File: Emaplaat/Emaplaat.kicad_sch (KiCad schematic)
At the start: 15 parts, among them IC1 ESP32-S3-WROOM-2-N32R16V, IC13 74HC595PW-Q100,118, IC7 74HC595PW-Q100,118

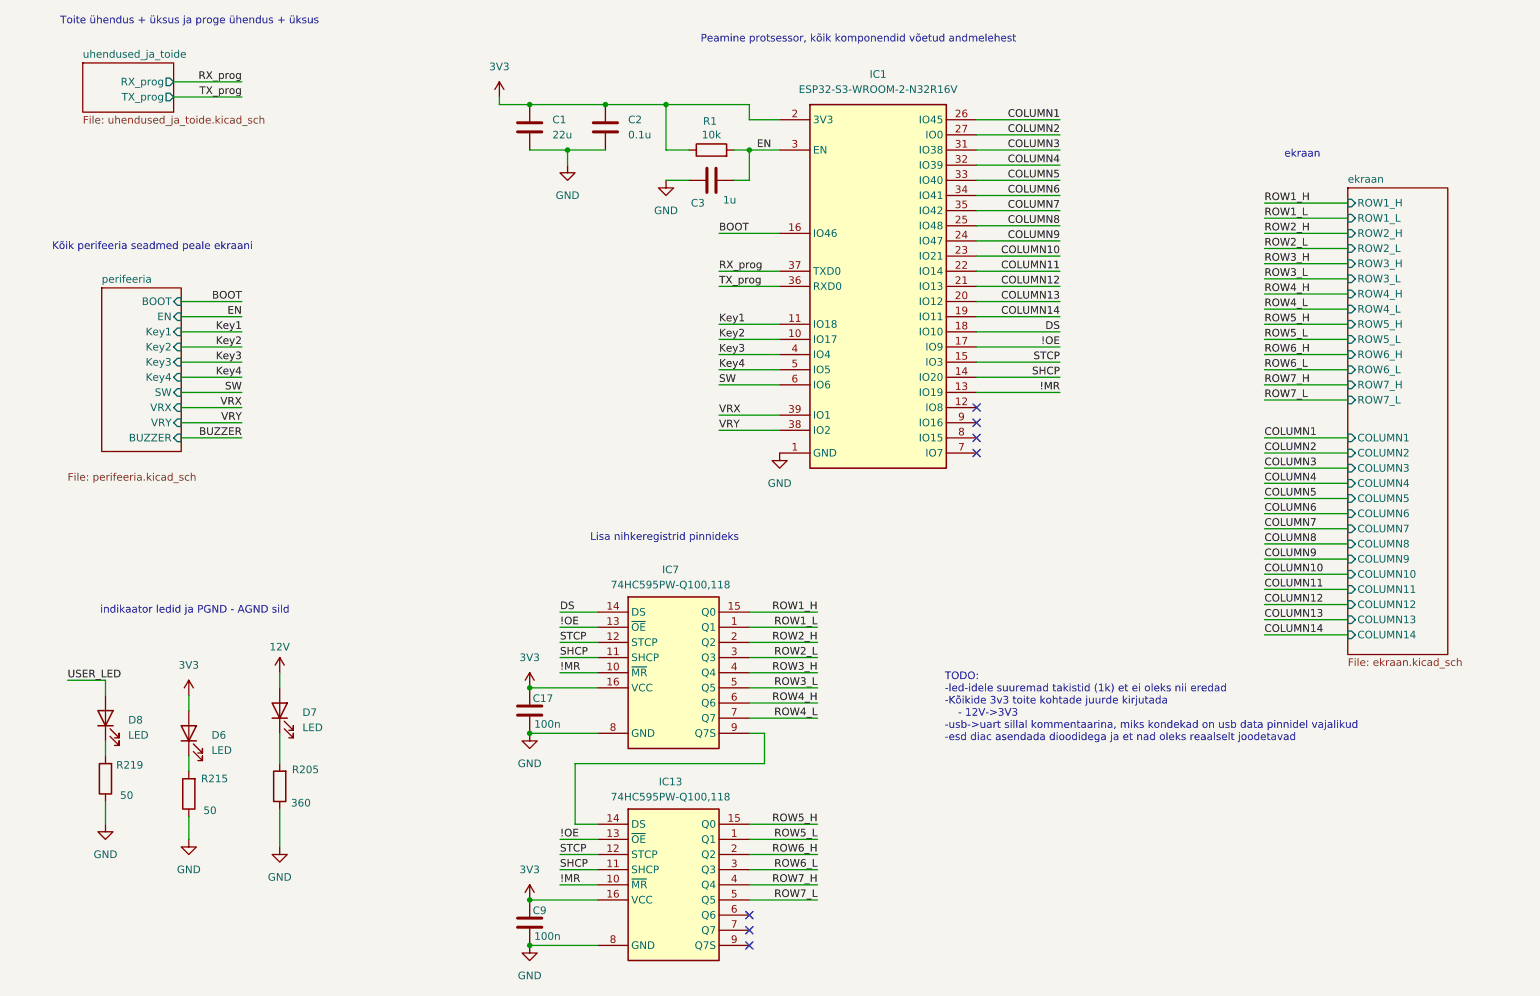
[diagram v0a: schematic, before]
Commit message: 3V3 voolud kontrollitud
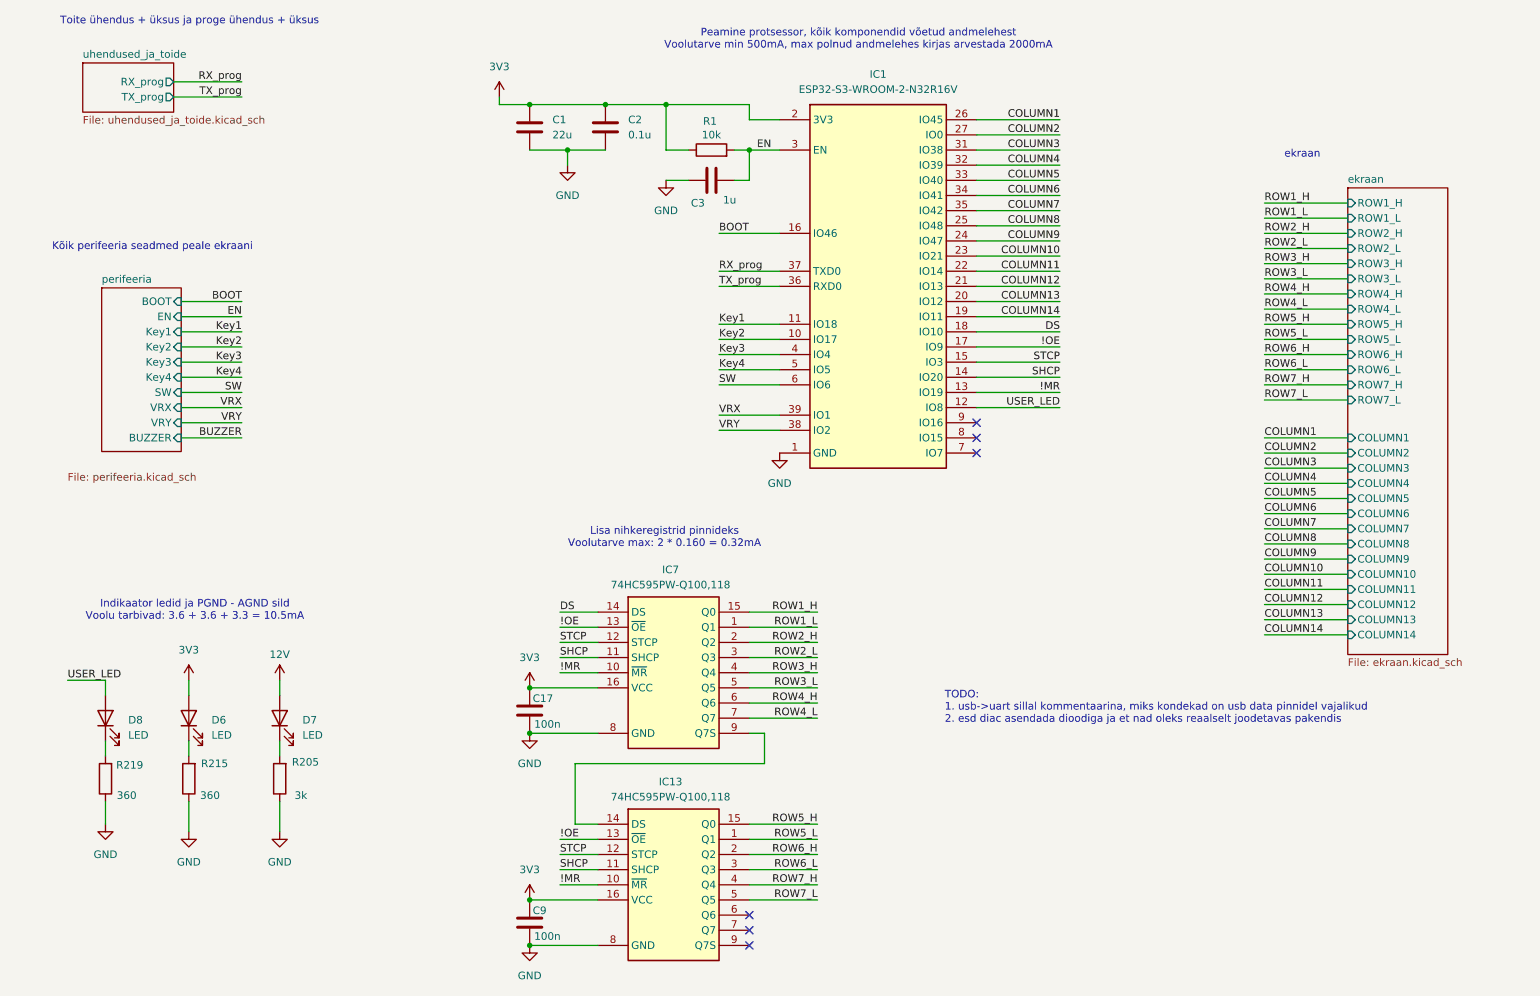
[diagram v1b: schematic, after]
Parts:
- R205: value 360 -> 3k
- R215, R219: value 50 -> 360
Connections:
- net USER_LED: now also IC1.12 (IO8)
- no-connect marks 7 -> 6
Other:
- note added: "Indikaator ledid ja PGND - AGND sild Voolu tarbivad: 3.6 + 3.6 + 3.3 = 10.5mA"
- note added: "Lisa nihkeregistrid pinnideks Voolutarve max: 2 * 0.160 = 0.32mA"
- note added: "Peamine protsessor, kõik komponendid võetud andmelehest Voolutarve min 500mA, max polnud andmelehes kirjas arvestada 2000mA"
- note added: "TODO: 1. usb->uart sillal kommentaarina, miks kondekad on usb data pinnidel vajalikud 2. esd diac asendada dioodiga ja et nad oleks reaalselt joodetavas pakendis"
- note removed: "Lisa nihkeregistrid pinnideks"
- note removed: "Peamine protsessor, kõik komponendid võetud andmelehest"
- note removed: "TODO: -led-idele suuremad takistid (1k) et ei oleks nii eredad -Kõikide 3v3 toite kohtade juurde kirjutada - 12V->3V3 -usb->uart sillal kommentaarina, miks kondekad on usb data pinnidel vajalikud -esd diac asendada dioodidega ja et nad oleks reaalselt joodetavad"
- note removed: "indikaator ledid ja PGND - AGND sild"
- moved on the sheet: D6, D7, R205, R215
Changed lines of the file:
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@@
 		)
 	)
-	(text "indikaator ledid ja PGND - AGND sild"
+	(text "Indikaator ledid ja PGND - AGND sild\nVoolu tarbivad: 3.6 + 3.6 + 3.3 = 10.5mA"
 		(exclude_from_sim no)
 		(at 53.086 128.016 0)
@@
 		)
 	)
-	(text "Peamine protsessor, kõik komponendid võetud andmelehest"
+	(text "Peamine protsessor, kõik komponendid võetud andmelehest\nVoolutarve min 500mA, max polnud andmelehes kirjas arvestada 2000mA"
 		(exclude_from_sim no)
 		(at 164.338 32.258 0)
@@
 		)
 	)
-	(text "Lisa nihkeregistrid pinnideks"
+	(text "Lisa nihkeregistrid pinnideks\nVoolutarve max: 2 * 0.160 = 0.32mA"
 		(exclude_from_sim no)
 		(at 131.826 115.824 0)
@@
 		)
 	)
-	(text "TODO:\n-led-idele suuremad takistid (1k) et ei oleks nii eredad\n-Kõikide 3v3 toite kohtade juurde kirjutada\n    - 12V->3V3\n-usb->uart sillal kommentaarina, miks kondekad on usb data pinnidel vajalikud\n-esd diac asendada dioodidega ja et nad oleks reaalselt joodetavad\n"
+	(text "TODO:\n1. usb->uart sillal kommentaarina, miks kondekad on usb data pinnidel vajalikud\n2. esd diac asendada dioodiga ja et nad oleks reaalselt joodetavas pakendis\n"
 		(exclude_from_sim no)
 		(at 178.816 144.272 0)
@@
 	)
 	(no_connect
-		(at 184.15 93.98)
-	)
-	(no_connect
 		(at 184.15 96.52)
 	)
@@
 	(wire
 		(pts
-			(xy 67.31 148.59) (xy 67.31 153.67)
+			(xy 67.31 149.86) (xy 67.31 152.4)
 		)
 		(stroke
@@
 	(wire
 		(pts
-			(xy 67.31 161.29) (xy 67.31 167.64)
+			(xy 67.31 160.02) (xy 67.31 165.1)
 		)
 		(stroke
@@
 	(wire
 		(pts
+			(xy 184.15 93.98) (xy 198.12 93.98)
+		)
+		(stroke
+			(width 0)
+			(type default)
+		)
+	)
+	(wire
+		(pts
 			(xy 232.41 67.31) (xy 246.38 67.31)
 		)
@@
 	(wire
 		(pts
-			(xy 67.31 138.43) (xy 67.31 140.97)
+			(xy 67.31 139.7) (xy 67.31 142.24)
 		)
 		(stroke
@@
 	(wire
 		(pts
-			(xy 52.07 152.4) (xy 52.07 154.94)
+			(xy 52.07 149.86) (xy 52.07 152.4)
 		)
 		(stroke
@@
 	(wire
 		(pts
-			(xy 52.07 162.56) (xy 52.07 166.37)
+			(xy 52.07 160.02) (xy 52.07 165.1)
 		)
 		(stroke
@@
 	(wire
 		(pts
-			(xy 52.07 144.78) (xy 52.07 142.24)
+			(xy 52.07 142.24) (xy 52.07 139.7)
 		)
 		(stroke
@@
 		)
 	)
+	(label "USER_LED"
+		(at 198.12 93.98 180)
+		(effects
+			(font
+				(size 1.27 1.27)
+			)
+			(justify right bottom)
+		)
+	)
 	(label "!MR"
 		(at 114.3 173.99 0)
@@
 	(symbol
 		(lib_id "power:VCC")
-		(at 67.31 138.43 0)
+		(at 67.31 139.7 0)
 		(unit 1)
 		(exclude_from_sim no)
@@
 		(dnp no)
 		(property "Reference" "#PWR0115"
-			(at 67.31 142.24 0)
+			(at 67.31 143.51 0)
 			(effects
 				(font
@@
 		)
 		(property "Value" "12V"
-			(at 67.31 134.112 0)
+			(at 67.31 135.382 0)
 			(effects
 				(font
@@
 		)
 		(property "Footprint" ""
-			(at 67.31 138.43 0)
+			(at 67.31 139.7 0)
 			(effects
 				(font
@@
 		)
 		(property "Datasheet" ""
-			(at 67.31 138.43 0)
+			(at 67.31 139.7 0)
 			(effects
 				(font
@@
 		)
 		(property "Description" "Power symbol creates a global label with name \"VCC\""
-			(at 67.31 138.43 0)
+			(at 67.31 139.7 0)
 			(effects
 				(font
@@
 	(symbol
 		(lib_id "Device:R")
-		(at 52.07 158.75 180)
+		(at 52.07 156.21 180)
 		(unit 1)
 		(exclude_from_sim no)
@@
 		(dnp no)
 		(property "Reference" "R215"
-			(at 56.388 156.21 0)
+			(at 56.388 153.67 0)
 			(effects
 				(font
@@
 			)
 		)
-		(property "Value" "50"
-			(at 55.626 161.544 0)
+		(property "Value" "360"
+			(at 55.626 159.004 0)
 			(effects
 				(font
@@
 		)
 		(property "Footprint" "Resistor_SMD:R_0603_1608Metric"
-			(at 53.848 158.75 90)
+			(at 53.848 156.21 90)
 			(effects
 				(font
@@
 		)
 		(property "Datasheet" "~"
-			(at 52.07 158.75 0)
+			(at 52.07 156.21 0)
 			(effects
 				(font
@@
 		)
 		(property "Description" "Resistor"
-			(at 52.07 158.75 0)
+			(at 52.07 156.21 0)
 			(effects
 				(font
@@
 	(symbol
 		(lib_id "Device:LED")
-		(at 52.07 148.59 90)
+		(at 52.07 146.05 90)
 		(unit 1)
 		(exclude_from_sim no)
@@
 		(dnp no)
 		(property "Reference" "D6"
-			(at 55.88 148.9074 90)
+			(at 55.88 146.3674 90)
 			(effects
 				(font
@@
 		)
 		(property "Value" "LED"
-			(at 55.88 151.4474 90)
+			(at 55.88 148.9074 90)
 			(effects
 				(font
@@
 		)
 		(property "Footprint" "LED_SMD:LED_0603_1608Metric"
-			(at 52.07 148.59 0)
+			(at 52.07 146.05 0)
 			(effects
 				(font
@@
 		)
 		(property "Datasheet" "https://www.we-online.com/components/products/datasheet/150060YS75000.pdf"
-			(at 52.07 148.59 0)
+			(at 52.07 146.05 0)
 			(effects
 				(font
@@
 		)
 		(property "Description" "Light emitting diode"
-			(at 52.07 148.59 0)
+			(at 52.07 146.05 0)
 			(effects
 				(font
@@
 		)
 		(property "Sim.Pins" "1=K 2=A"
-			(at 52.07 148.59 0)
+			(at 52.07 146.05 0)
 			(effects
 				(font
@@
 	(symbol
 		(lib_id "power:GND")
-		(at 52.07 166.37 0)
+		(at 52.07 165.1 0)
 		(unit 1)
 		(exclude_from_sim no)
@@
 		(fields_autoplaced yes)
 		(property "Reference" "#PWR021"
-			(at 52.07 172.72 0)
+			(at 52.07 171.45 0)
 			(effects
 				(font
@@
 		)
 		(property "Value" "GND"
-			(at 52.07 171.45 0)
+			(at 52.07 170.18 0)
 			(effects
 				(font
@@
 		)
 		(property "Footprint" ""
-			(at 52.07 166.37 0)
+			(at 52.07 165.1 0)
 			(effects
 				(font
@@
 		)
 		(property "Datasheet" ""
-			(at 52.07 166.37 0)
+			(at 52.07 165.1 0)
 			(effects
 				(font
@@
 		)
 		(property "Description" "Power symbol creates a global label with name \"GND\" , ground"
-			(at 52.07 166.37 0)
+			(at 52.07 165.1 0)
 			(effects
 				(font
@@
 	(symbol
 		(lib_id "Device:R")
-		(at 67.31 157.48 180)
+		(at 67.31 156.21 180)
 		(unit 1)
 		(exclude_from_sim no)
@@
 		(dnp no)
 		(property "Reference" "R205"
-			(at 71.628 154.686 0)
+			(at 71.628 153.416 0)
 			(effects
 				(font
@@
 			)
 		)
-		(property "Value" "360"
-			(at 70.866 160.274 0)
+		(property "Value" "3k"
+			(at 70.866 159.004 0)
 			(effects
 				(font
@@
 		)
 		(property "Footprint" "Resistor_SMD:R_0603_1608Metric"
-			(at 69.088 157.48 90)
+			(at 69.088 156.21 90)
 			(effects
 				(font
@@
 		)
 		(property "Datasheet" "~"
-			(at 67.31 157.48 0)
+			(at 67.31 156.21 0)
 			(effects
 				(font
@@
 		)
 		(property "Description" "Resistor"
-			(at 67.31 157.48 0)
+			(at 67.31 156.21 0)
 			(effects
 				(font
@@
 	(symbol
 		(lib_id "power:GND")
-		(at 67.31 167.64 0)
+		(at 67.31 165.1 0)
 		(unit 1)
 		(exclude_from_sim no)
@@
 		(fields_autoplaced yes)
 		(property "Reference" "#PWR020"
-			(at 67.31 173.99 0)
+			(at 67.31 171.45 0)
 			(effects
 				(font
@@
 		)
 		(property "Value" "GND"
-			(at 67.31 172.72 0)
+			(at 67.31 170.18 0)
 			(effects
 				(font
@@
 		)
 		(property "Footprint" ""
-			(at 67.31 167.64 0)
+			(at 67.31 165.1 0)
 			(effects
 				(font
@@
 		)
 		(property "Datasheet" ""
-			(at 67.31 167.64 0)
+			(at 67.31 165.1 0)
 			(effects
 				(font
@@
 		)
 		(property "Description" "Power symbol creates a global label with name \"GND\" , ground"
-			(at 67.31 167.64 0)
+			(at 67.31 165.1 0)
 			(effects
 				(font
@@
 			)
 		)
-		(property "Value" "50"
+		(property "Value" "360"
 			(at 41.656 159.004 0)
 			(effects
@@
 	(symbol
 		(lib_id "Device:LED")
-		(at 67.31 144.78 90)
+		(at 67.31 146.05 90)
 		(unit 1)
 		(exclude_from_sim no)
@@
 		(fields_autoplaced yes)
 		(property "Reference" "D7"
-			(at 71.12 145.0974 90)
+			(at 71.12 146.3674 90)
 			(effects
 				(font
@@
 		)
 		(property "Value" "LED"
-			(at 71.12 147.6374 90)
+			(at 71.12 148.9074 90)
 			(effects
 				(font
@@
 		)
 		(property "Footprint" "LED_SMD:LED_0603_1608Metric"
-			(at 67.31 144.78 0)
+			(at 67.31 146.05 0)
 			(effects
 				(font
@@
 		)
 		(property "Datasheet" "https://www.we-online.com/components/products/datasheet/150060YS75000.pdf"
-			(at 67.31 144.78 0)
+			(at 67.31 146.05 0)
 			(effects
 				(font
@@
 		)
 		(property "Description" "Light emitting diode"
-			(at 67.31 144.78 0)
+			(at 67.31 146.05 0)
 			(effects
 				(font
@@
 		)
 		(property "Sim.Pins" "1=K 2=A"
-			(at 67.31 144.78 0)
+			(at 67.31 146.05 0)
 			(effects
 				(font
@@
 	(symbol
 		(lib_id "power:VCC")
-		(at 52.07 142.24 0)
+		(at 52.07 139.7 0)
 		(unit 1)
 		(exclude_from_sim no)
@@
 		(fields_autoplaced yes)
 		(property "Reference" "#PWR0113"
-			(at 52.07 146.05 0)
+			(at 52.07 143.51 0)
 			(effects
 				(font
@@
 		)
 		(property "Value" "3V3"
-			(at 52.07 137.16 0)
+			(at 52.07 134.62 0)
 			(effects
 				(font
@@
 		)
 		(property "Footprint" ""
-			(at 52.07 142.24 0)
+			(at 52.07 139.7 0)
 			(effects
 				(font
@@
 		)
 		(property "Datasheet" ""
-			(at 52.07 142.24 0)
+			(at 52.07 139.7 0)
 			(effects
 				(font
@@
 		)
 		(property "Description" "Power symbol creates a global label with name \"VCC\""
-			(at 52.07 142.24 0)
+			(at 52.07 139.7 0)
 			(effects
 				(font

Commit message: Kaareli kolmas tagasiside
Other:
- note removed: "TODO: 1. usb->uart sillal kommentaarina, miks kondekad on usb data pinnidel vajalikud 2. esd diac asendada dioodiga ja et nad oleks reaalselt joodetavas pakendis"
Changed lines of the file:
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@@
-		)
-	)
-	(text "TODO:\n1. usb->uart sillal kommentaarina, miks kondekad on usb data pinnidel vajalikud\n2. esd diac asendada dioodiga ja et nad oleks reaalselt joodetavas pakendis\n"
-		(exclude_from_sim no)
-		(at 178.816 144.272 0)
-		(effects
-			(font
-				(size 1.27 1.27)
-			)
-			(justify left)
 		)
 	)

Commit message: jajald
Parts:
- C1, C2, C3: footprint (none) -> Capacitor_SMD:C_0603_1608Metric_Pad1.08x0.95mm_HandSolder
- C4: renamed from C17; footprint (none) -> Capacitor_SMD:C_0603_1608Metric_Pad1.08x0.95mm_HandSolder
- C5: renamed from C9; footprint (none) -> Capacitor_SMD:C_0603_1608Metric_Pad1.08x0.95mm_HandSolder
- D1: renamed from D8; footprint LED_SMD:LED_0603_1608Metric -> LED_SMD:LED_0603_1608Metric_Pad1.05x0.95mm_HandSolder
- D2: renamed from D6; footprint LED_SMD:LED_0603_1608Metric -> LED_SMD:LED_0603_1608Metric_Pad1.05x0.95mm_HandSolder
- D3: renamed from D7; footprint LED_SMD:LED_0603_1608Metric -> LED_SMD:LED_0603_1608Metric_Pad1.05x0.95mm_HandSolder
- R1: footprint (none) -> Resistor_SMD:R_0603_1608Metric_Pad0.98x0.95mm_HandSolder
- R2: renamed from R219; footprint Resistor_SMD:R_0603_1608Metric -> Resistor_SMD:R_0603_1608Metric_Pad0.98x0.95mm_HandSolder
- R3: renamed from R215; footprint Resistor_SMD:R_0603_1608Metric -> Resistor_SMD:R_0603_1608Metric_Pad0.98x0.95mm_HandSolder
- R4: renamed from R205; footprint Resistor_SMD:R_0603_1608Metric -> Resistor_SMD:R_0603_1608Metric_Pad0.98x0.95mm_HandSolder
- renumbered IC7 to IC2, IC13 to IC3
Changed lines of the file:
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@@
 			)
 		)
-		(property "Footprint" ""
+		(property "Footprint" "Capacitor_SMD:C_0603_1608Metric_Pad1.08x0.95mm_HandSolder"
 			(at 110.1852 50.8 0)
 			(effects
@@
 		(on_board yes)
 		(dnp no)
-		(property "Reference" "D8"
+		(property "Reference" "D1"
 			(at 41.91 146.3674 90)
 			(effects
@@
 			)
 		)
-		(property "Footprint" "LED_SMD:LED_0603_1608Metric"
+		(property "Footprint" "LED_SMD:LED_0603_1608Metric_Pad1.05x0.95mm_HandSolder"
 			(at 38.1 146.05 0)
 			(effects
@@
 			(project "Emaplaat"
 				(path "/489224c0-ace1-4530-aa61-a5d03adf1434"
-					(reference "D8")
+					(reference "D1")
 					(unit 1)
 				)
@@
 			)
 		)
-		(property "Footprint" ""
+		(property "Footprint" "Capacitor_SMD:C_0603_1608Metric_Pad1.08x0.95mm_HandSolder"
 			(at 122.8852 50.8 0)
 			(effects
@@
 		(dnp no)
 		(fields_autoplaced yes)
-		(property "Reference" "IC7"
+		(property "Reference" "IC2"
 			(at 132.842 121.158 0)
 			(effects
@@
 			(project "Emaplaat"
 				(path "/489224c0-ace1-4530-aa61-a5d03adf1434"
-					(reference "IC7")
+					(reference "IC2")
 					(unit 1)
 				)
@@
 		(on_board yes)
 		(dnp no)
-		(property "Reference" "R215"
+		(property "Reference" "R3"
 			(at 56.388 153.67 0)
 			(effects
@@
 			)
 		)
-		(property "Footprint" "Resistor_SMD:R_0603_1608Metric"
+		(property "Footprint" "Resistor_SMD:R_0603_1608Metric_Pad0.98x0.95mm_HandSolder"
 			(at 53.848 156.21 90)
 			(effects
@@
 			(project "Emaplaat"
 				(path "/489224c0-ace1-4530-aa61-a5d03adf1434"
-					(reference "R215")
+					(reference "R3")
 					(unit 1)
 				)
@@
 		(on_board yes)
 		(dnp no)
-		(property "Reference" "D6"
+		(property "Reference" "D2"
 			(at 55.88 146.3674 90)
 			(effects
@@
 			)
 		)
-		(property "Footprint" "LED_SMD:LED_0603_1608Metric"
+		(property "Footprint" "LED_SMD:LED_0603_1608Metric_Pad1.05x0.95mm_HandSolder"
 			(at 52.07 146.05 0)
 			(effects
@@
 			(project "Emaplaat"
 				(path "/489224c0-ace1-4530-aa61-a5d03adf1434"
-					(reference "D6")
+					(reference "D2")
 					(unit 1)
 				)
@@
 			)
 		)
-		(property "Footprint" ""
+		(property "Footprint" "Capacitor_SMD:C_0603_1608Metric_Pad1.08x0.95mm_HandSolder"
 			(at 143.51 54.9148 0)
 			(effects
@@
 		(dnp no)
 		(fields_autoplaced yes)
-		(property "Reference" "IC13"
+		(property "Reference" "IC3"
 			(at 132.842 156.718 0)
 			(effects
@@
 			(project "Emaplaat"
 				(path "/489224c0-ace1-4530-aa61-a5d03adf1434"
-					(reference "IC13")
+					(reference "IC3")
 					(unit 1)
 				)
@@
 		(on_board yes)
 		(dnp no)
-		(property "Reference" "R205"
+		(property "Reference" "R4"
 			(at 71.628 153.416 0)
 			(effects
@@
 			)
 		)
-		(property "Footprint" "Resistor_SMD:R_0603_1608Metric"
+		(property "Footprint" "Resistor_SMD:R_0603_1608Metric_Pad0.98x0.95mm_HandSolder"
 			(at 69.088 156.21 90)
 			(effects
@@
 			(project "Emaplaat"
 				(path "/489224c0-ace1-4530-aa61-a5d03adf1434"
-					(reference "R205")
+					(reference "R4")
 					(unit 1)
 				)
@@
 			)
 		)
-		(property "Footprint" ""
+		(property "Footprint" "Resistor_SMD:R_0603_1608Metric_Pad0.98x0.95mm_HandSolder"
 			(at 139.7 52.578 90)
 			(effects
@@
 		(on_board yes)
 		(dnp no)
-		(property "Reference" "C17"
+		(property "Reference" "C4"
 			(at 109.728 142.748 0)
 			(effects
@@
 			)
 		)
-		(property "Footprint" ""
+		(property "Footprint" "Capacitor_SMD:C_0603_1608Metric_Pad1.08x0.95mm_HandSolder"
 			(at 110.1852 148.59 0)
 			(effects
@@
 			(project "Emaplaat"
 				(path "/489224c0-ace1-4530-aa61-a5d03adf1434"
-					(reference "C17")
+					(reference "C4")
 					(unit 1)
 				)
@@
 		(on_board yes)
 		(dnp no)
-		(property "Reference" "R219"
+		(property "Reference" "R2"
 			(at 42.164 153.924 0)
 			(effects
@@
 			)
 		)
-		(property "Footprint" "Resistor_SMD:R_0603_1608Metric"
+		(property "Footprint" "Resistor_SMD:R_0603_1608Metric_Pad0.98x0.95mm_HandSolder"
 			(at 39.878 156.21 90)
 			(effects
@@
 			(project "Emaplaat"
 				(path "/489224c0-ace1-4530-aa61-a5d03adf1434"
-					(reference "R219")
+					(reference "R2")
 					(unit 1)
 				)
@@
 		(dnp no)
 		(fields_autoplaced yes)
-		(property "Reference" "D7"
+		(property "Reference" "D3"
 			(at 71.12 146.3674 90)
 			(effects
@@
 			)
 		)
-		(property "Footprint" "LED_SMD:LED_0603_1608Metric"
+		(property "Footprint" "LED_SMD:LED_0603_1608Metric_Pad1.05x0.95mm_HandSolder"
 			(at 67.31 146.05 0)
 			(effects
@@
 			(project "Emaplaat"
 				(path "/489224c0-ace1-4530-aa61-a5d03adf1434"
-					(reference "D7")
+					(reference "D3")
 					(unit 1)
 				)
@@
 		(on_board yes)
 		(dnp no)
-		(property "Reference" "C9"
+		(property "Reference" "C5"
 			(at 109.728 178.308 0)
 			(effects
@@
 			)
 		)
-		(property "Footprint" ""
+		(property "Footprint" "Capacitor_SMD:C_0603_1608Metric_Pad1.08x0.95mm_HandSolder"
 			(at 110.1852 184.15 0)
 			(effects
@@
 			(project "Emaplaat"
 				(path "/489224c0-ace1-4530-aa61-a5d03adf1434"
-					(reference "C9")
-					(unit 1)
-				)
+					(reference "C5")
+					(unit 1)
+				)
